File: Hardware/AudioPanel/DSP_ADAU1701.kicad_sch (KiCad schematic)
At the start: 33 parts, among them Q1 FZT953, U104 ADAU1701, Y2 12.288 MHz

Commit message: small stuff
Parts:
- renumbered C439 to C179, C440 to C180, C448 to C181, C447 to C182, C458 to C183, C449 to C184, C459 to C185, C445 to C186, C452 to C187, C446 to C188, C444 to C189, C453 to C190, C450 to C191, C454 to C192, C451 to C193, C456 to C194, C455 to C195, C438 to C196, C442 to C197, C441 to C198, C443 to C199, C457 to C200, JP1 to JP4, Q1 to Q4, R291 to R103, R295 to R212, R296 to R213, R294 to R214, R293 to R215, R292 to R216, R297 to R217, U104 to U58, Y2 to Y6

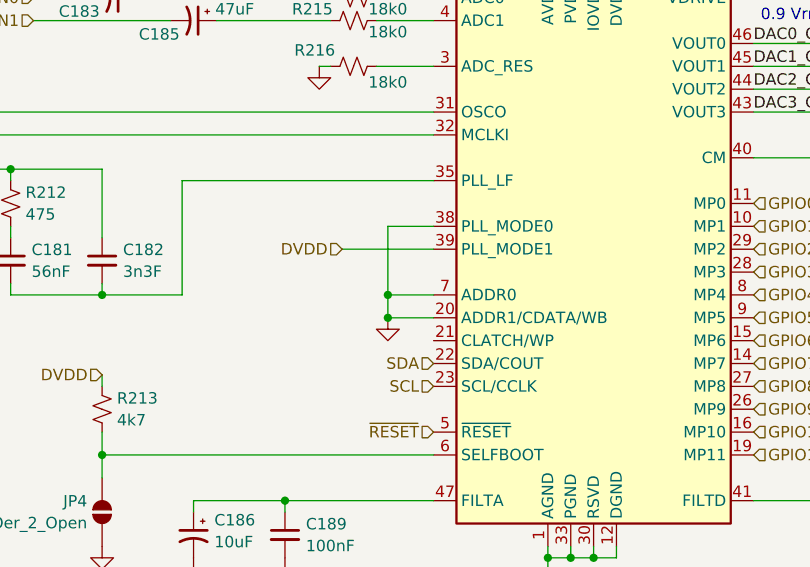
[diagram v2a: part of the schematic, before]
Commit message: Adding ADAV400 sheet
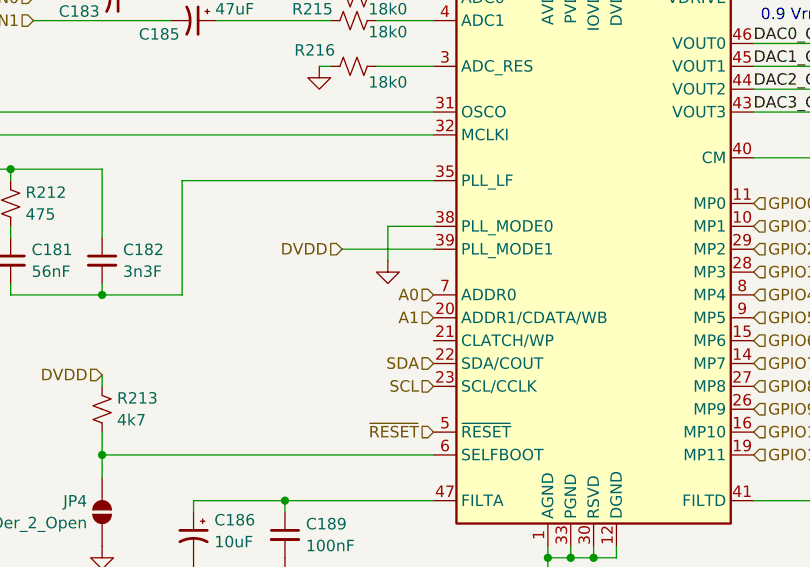
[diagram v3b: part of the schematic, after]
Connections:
- net GND: no longer U58.20 (ADDR1/CDATA/WB), U58.7 (ADDR0)
- new net A0: U58.7 (ADDR0)
- new net A1: U58.20 (ADDR1/CDATA/WB)

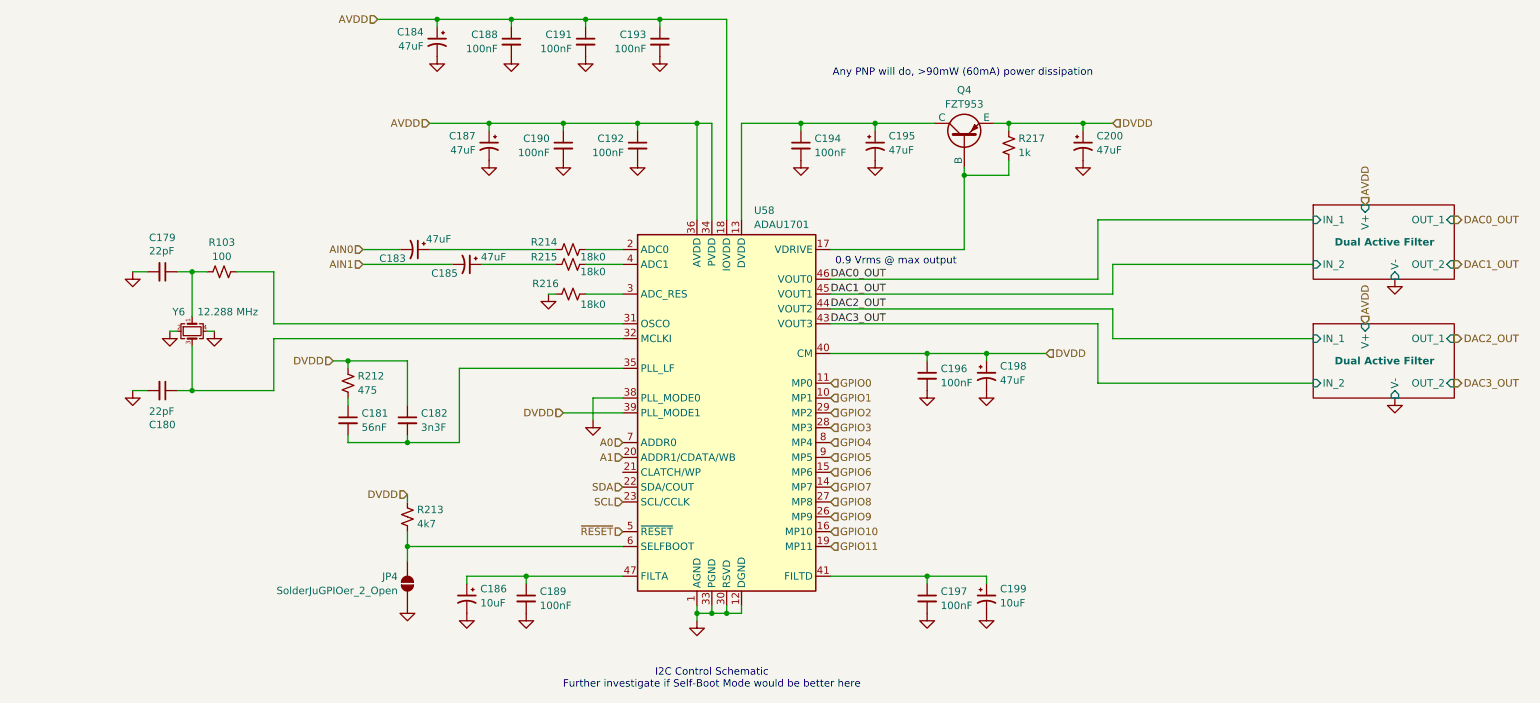
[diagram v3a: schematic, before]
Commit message: Realized that I need to rethink how I'm going to mix the radio audio with the stereo audio
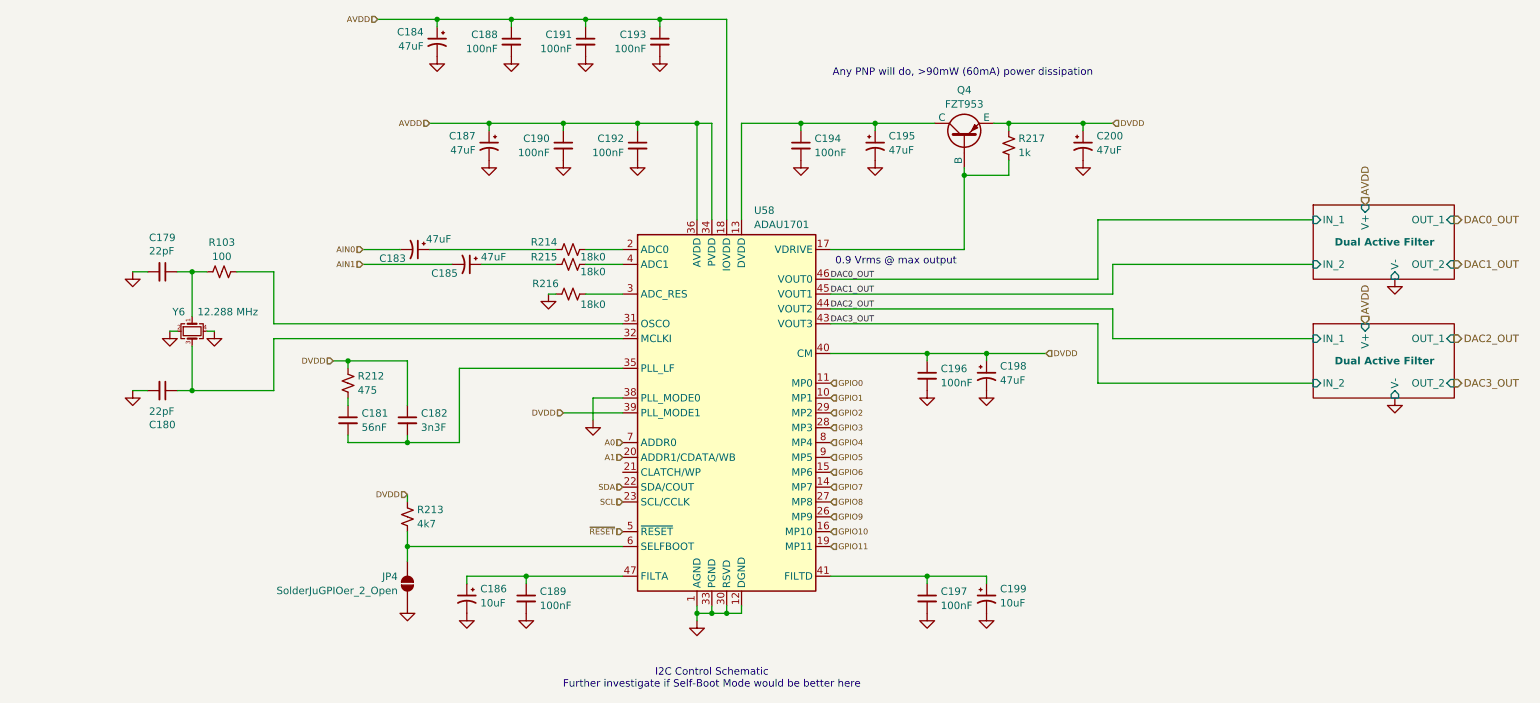
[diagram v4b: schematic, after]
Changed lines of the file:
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@@
 		(effects
 			(font
-				(size 1.27 1.27)
+				(size 1 1)
 			)
 			(justify left bottom)
@@
 		(effects
 			(font
-				(size 1.27 1.27)
+				(size 1 1)
 			)
 			(justify left bottom)
@@
 		(effects
 			(font
-				(size 1.27 1.27)
+				(size 1 1)
 			)
 			(justify left bottom)
@@
 		(effects
 			(font
-				(size 1.27 1.27)
+				(size 1 1)
 			)
 			(justify left bottom)
@@
 		(effects
 			(font
-				(size 1.27 1.27)
+				(size 1 1)
 			)
 			(justify left)
@@
 		(effects
 			(font
-				(size 1.27 1.27)
+				(size 1 1)
 			)
 			(justify left)
@@
 		(effects
 			(font
-				(size 1.27 1.27)
+				(size 1 1)
 			)
 			(justify right)
@@
 		(effects
 			(font
-				(size 1.27 1.27)
+				(size 1 1)
 			)
 			(justify right)
@@
 		(effects
 			(font
-				(size 1.27 1.27)
+				(size 1 1)
 			)
 			(justify right)
@@
 		(effects
 			(font
-				(size 1.27 1.27)
+				(size 1 1)
 			)
 			(justify right)
@@
 		(effects
 			(font
-				(size 1.27 1.27)
+				(size 1 1)
 			)
 			(justify right)
@@
 		(effects
 			(font
-				(size 1.27 1.27)
+				(size 1 1)
 			)
 			(justify right)
@@
 		(effects
 			(font
-				(size 1.27 1.27)
+				(size 1 1)
 			)
 			(justify right)
@@
 		(effects
 			(font
-				(size 1.27 1.27)
+				(size 1 1)
 			)
 			(justify left)
@@
 		(effects
 			(font
-				(size 1.27 1.27)
+				(size 1 1)
 			)
 			(justify left)
@@
 		(effects
 			(font
-				(size 1.27 1.27)
+				(size 1 1)
 			)
 			(justify left)
@@
 		(effects
 			(font
-				(size 1.27 1.27)
+				(size 1 1)
 			)
 			(justify left)
@@
 		(effects
 			(font
-				(size 1.27 1.27)
+				(size 1 1)
 			)
 			(justify left)
@@
 		(effects
 			(font
-				(size 1.27 1.27)
+				(size 1 1)
 			)
 			(justify right)
@@
 		(effects
 			(font
-				(size 1.27 1.27)
+				(size 1 1)
 			)
 			(justify left)
@@
 		(effects
 			(font
-				(size 1.27 1.27)
+				(size 1 1)
 			)
 			(justify left)
@@
 		(effects
 			(font
-				(size 1.27 1.27)
+				(size 1 1)
 			)
 			(justify left)
@@
 		(effects
 			(font
-				(size 1.27 1.27)
+				(size 1 1)
 			)
 			(justify left)
@@
 		(effects
 			(font
-				(size 1.27 1.27)
+				(size 1 1)
 			)
 			(justify right)
@@
 		(effects
 			(font
-				(size 1.27 1.27)
+				(size 1 1)
 			)
 			(justify left)
@@
 		(effects
 			(font
-				(size 1.27 1.27)
+				(size 1 1)
 			)
 			(justify left)
@@
 		(effects
 			(font
-				(size 1.27 1.27)
+				(size 1 1)
 			)
 			(justify left)
@@
 		(effects
 			(font
-				(size 1.27 1.27)
+				(size 1 1)
 			)
 			(justify right)
@@
 		(effects
 			(font
-				(size 1.27 1.27)
+				(size 1 1)
 			)
 			(justify right)
@@
 		(effects
 			(font
-				(size 1.27 1.27)
-			)
-			(justify right)
+				(size 1 1)
+			)
+			(justify right)

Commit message: Added MT8816 for audio switching
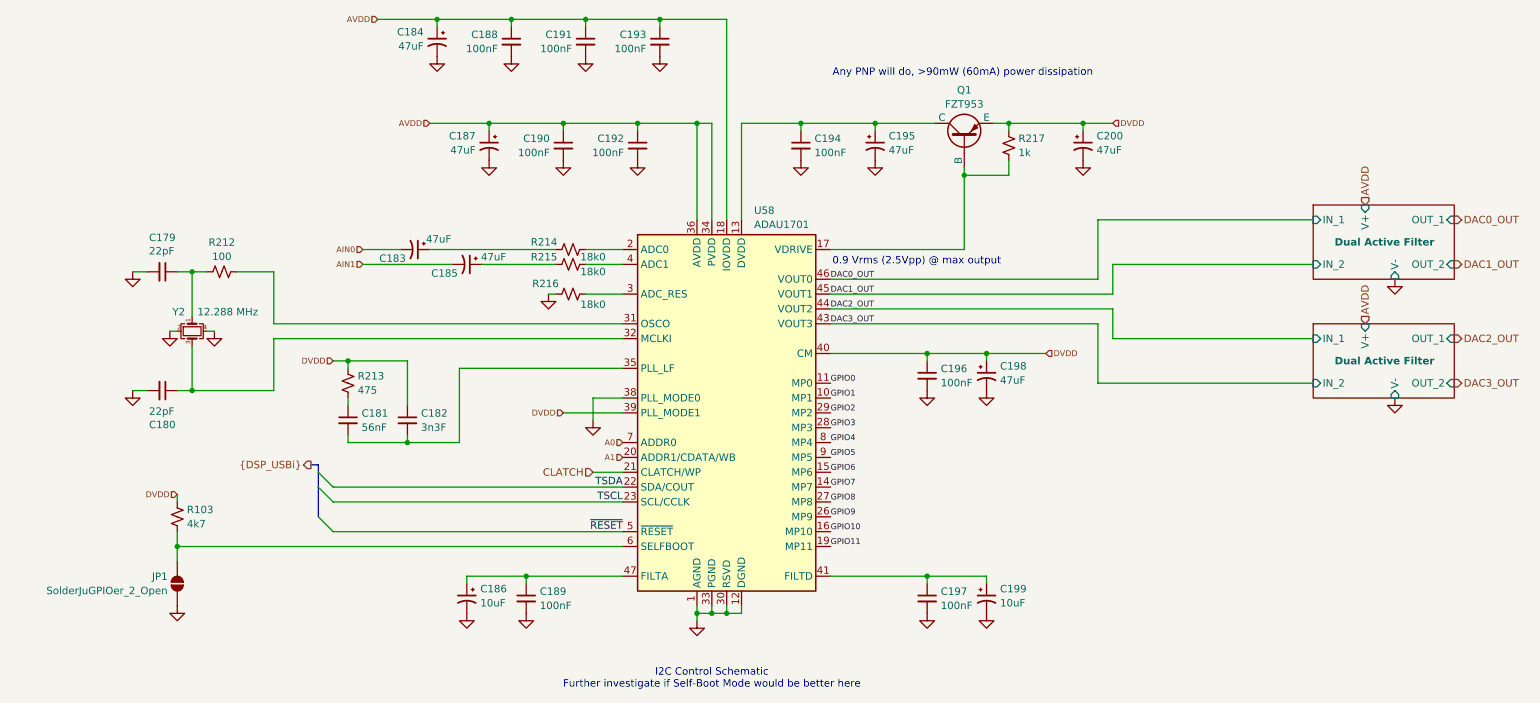
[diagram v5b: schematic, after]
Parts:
- renumbered JP4 to JP1, Q4 to Q1, R213 to R103, R103 to R212, R212 to R213, Y6 to Y2
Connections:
- net CLATCH: now reaches U58.21 (CLATCH/WP)
- net SCL renamed TSCL
- net SDA renamed TSDA
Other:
- note added: "0.9 Vrms (2.5Vpp) @ max output"
- note removed: "0.9 Vrms @ max output"
- moved on the sheet: JP1, R103

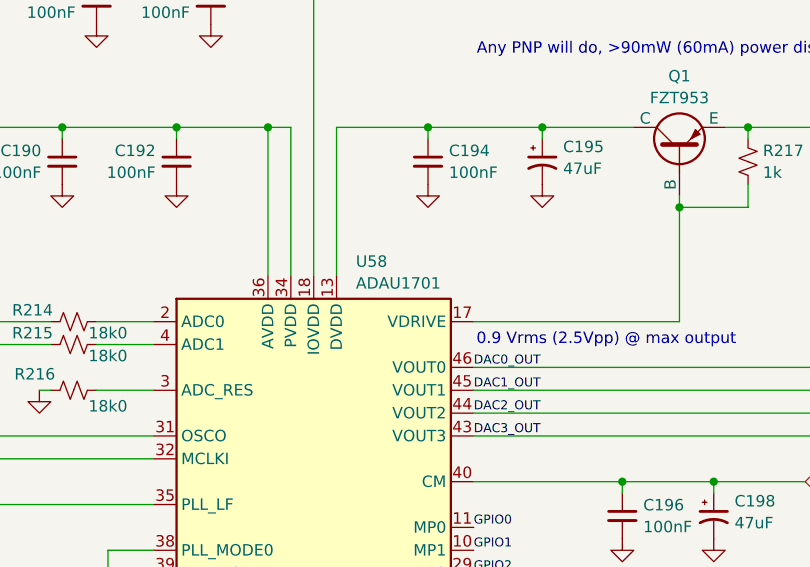
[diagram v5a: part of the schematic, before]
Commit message: Adjusted MIC input to crosspoint switch
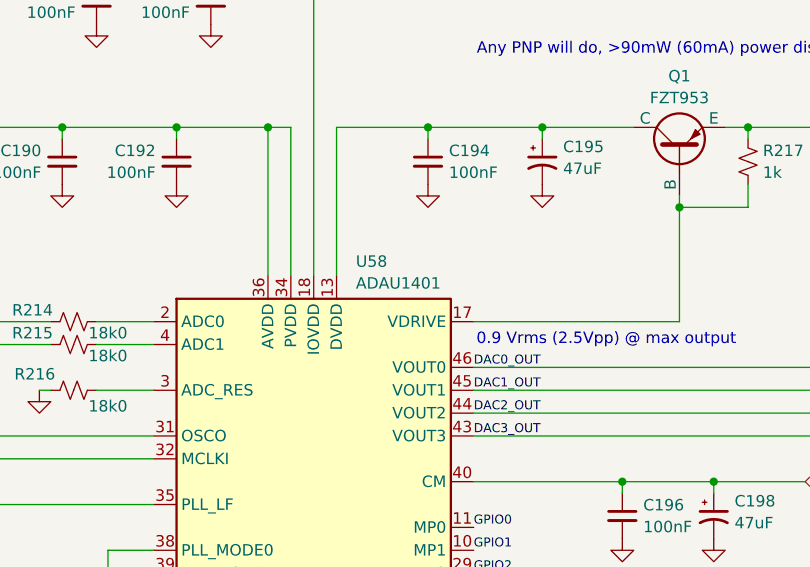
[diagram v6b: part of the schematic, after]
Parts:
- U58: value ADAU1701 -> ADAU1401
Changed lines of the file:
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@@
 			)
 		)
-		(property "Value" "ADAU1701"
+		(property "Value" "ADAU1401"
 			(at 149.4633 120.1998 0)
 			(effects
